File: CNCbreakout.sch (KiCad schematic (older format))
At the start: 90 parts, among them P1 X1, P10 XY_STOP, P11 Z_STOP, P2 X2, P3 Y, P4 Z, P5 VFD_IN, Q1 Q_NPN_CBE, Q10 Q_NPN_CBE, Q12 Q_NPN_CBE, Q2 Q_NPN_CBE, Q3 Q_NPN_CBE, Q4 Q_NPN_CBE, Q6 Q_NPN_CBE, Q8 Q_NPN_CBE

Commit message: added spindle hall, assignd footprints
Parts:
- removed P?: CONN_01X06, symbol CONN_01X06
- added P12: +24V, Connect:bornier2, symbol CONN_01X02
- added P6: VFD_GP1, Connect:bornier2, symbol CONN_01X02
- added P7: VFD_GP2, Connect:bornier2, symbol CONN_01X02
- added P8: VFD_GP3, Connect:bornier2, symbol CONN_01X02
- added P9: GND, Connect:bornier2, symbol CONN_01X02
- added R45, R46: 10K, Resistors_SMD:R_1206, symbol R
- added R50, R51: 100K, Resistors_SMD:R_1206, symbol R
- added U1, U2: 4N25, Opto-Devices:Optocoupler_SMD_ReflowWaveSoldering_KPC357_LTV35x_PC357_SingleChannel, symbol 4N25
- D1, D10, D11, D12, D2, D3, D4, D5, D6, D7, D8, D9: footprint (none) -> LEDs:LED_1206
- D13, D14, D15, D16, D17, D18, D19, D20, D21: renamed from D?; footprint (none) -> LEDs:LED_1206
- P1, P2, P3, P4: footprint (none) -> Connect:DB9FC
- Q1, Q10, Q12, Q2, Q3, Q4, Q6, Q8: footprint (none) -> TO_SOT_Packages_SMD:SOT-23
- Q11, Q13, Q14, Q5, Q7, Q9: renamed from Q?; footprint (none) -> TO_SOT_Packages_SMD:TO-252-2Lead
- R1, R10, R11, R12, R13, R14, R15, R16, R17, R18, R19, R2, R20, R21, R22, R23, R24, R25, R26, R27, R28, R29, R3, R30, R31, R32, R33, R34, R35, R36, R37, R38, R39, R4, R40, R41, R42, R43, R44, R47, R48, R49, R5, R6, R7, R8, R9: renamed from R?; footprint (none) -> Resistors_SMD:R_1206
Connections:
- net labels added: DGND
- net labels removed: ServoOn_CON, ServoOn_PC
- wire segments 216 -> 235
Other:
- note added: "ACS806 Limit switches are 5K NPN base signals intended for 5V."
- note added: "KRS limit switches are optos intended for Open Collector"
- note added: "Servo enable is left to the FPGA."
- note removed: "ACS806 Limit switches are 5V TTL signals."
- note removed: "Intercept the Servo-On signal\nhere to let the safety controller\npower it down."
- note removed: "KRS limit switches are Open Collector"

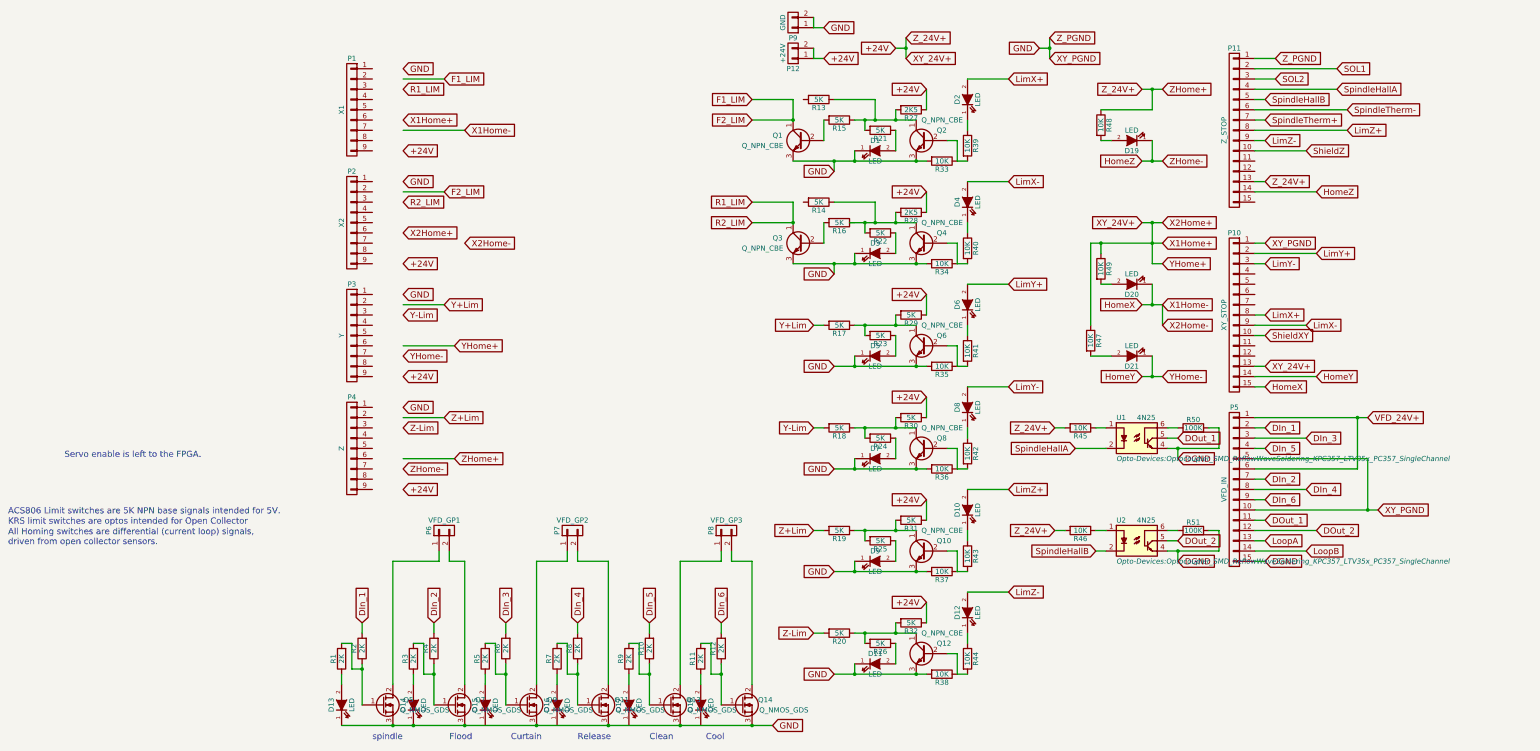
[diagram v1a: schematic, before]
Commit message: cleanup and added enable intercept
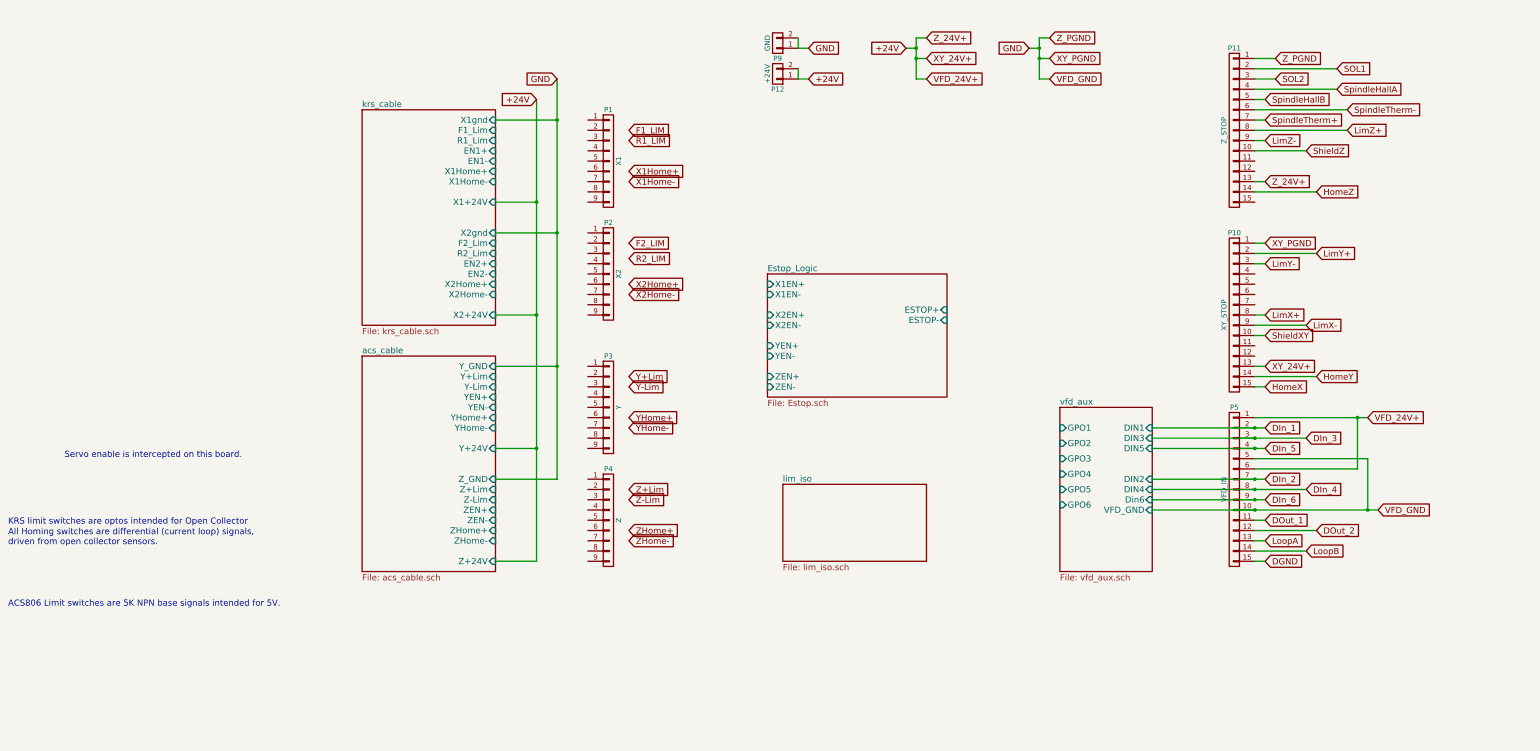
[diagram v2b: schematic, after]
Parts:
- removed D1, D10, D11, D12, D13, D14, D15, D16, D17, D18, D19, D2, D20, D21, D3, D4, D5, D6, D7, D8, D9: LED, LEDs:LED_1206, symbol LED
- removed P6: VFD_GP1, Connect:bornier2, symbol CONN_01X02
- removed P7: VFD_GP2, Connect:bornier2, symbol CONN_01X02
- removed P8: VFD_GP3, Connect:bornier2, symbol CONN_01X02
- removed Q1, Q10, Q12, Q2, Q3, Q4, Q6, Q8: Q_NPN_CBE, TO_SOT_Packages_SMD:SOT-23, symbol Q_NPN_CBE
- removed Q11, Q13, Q14, Q5, Q7, Q9: Q_NMOS_GDS, TO_SOT_Packages_SMD:TO-252-2Lead, symbol Q_NMOS_GDS
- removed R1, R10, R11, R12, R2, R3, R4, R5, R6, R7, R8, R9: 2K, Resistors_SMD:R_1206, symbol R
- removed R13, R14, R15, R16, R17, R18, R19, R20, R21, R22, R23, R24, R25, R26, R29, R30, R31, R32: 5K, Resistors_SMD:R_1206, symbol R
- removed R27, R28: 2K5, Resistors_SMD:R_1206, symbol R
- removed R33, R34, R35, R36, R37, R38, R39, R40, R41, R42, R43, R44, R45, R46, R47, R48, R49: 10K, Resistors_SMD:R_1206, symbol R
- removed R50, R51: 100K, Resistors_SMD:R_1206, symbol R
- removed U1, U2: 4N25, Opto-Devices:Optocoupler_SMD_ReflowWaveSoldering_KPC357_LTV35x_PC357_SingleChannel, symbol 4N25
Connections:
- net VFD_24V+ is gone; now on net +24V: P5.1 (P1), P5.6 (P6)
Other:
- note added: "Servo enable is intercepted on this board."
- note removed: "Clean"
- note removed: "Cool"
- note removed: "Curtain"
- note removed: "Flood"
- note removed: "Release"
- note removed: "Servo enable is left to the FPGA."
- note removed: "spindle"
- moved on the sheet: P1, P12, P2, P3, P4, P9

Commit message: started pcb layout
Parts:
- added P110, P111, P112: CONN_01X02, Connect:bornier2, symbol CONN_01X02
- renumbered P1 to P101, P2 to P102, P3 to P103, P4 to P104, P9 to P105, P12 to P106, P11 to P107, P10 to P108, P5 to P109
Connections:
- net +24V: now also P101.9 (P9), P102.9 (P9), P103.9 (P9), P104.9 (P9)
- net F1_LIM: now also P101.2 (P2)
- net F2_LIM: now also P102.2 (P2)
- net GND: now also P101.1 (P1), P102.1 (P1), P103.1 (P1), P104.1 (P1)
- net R1_LIM: now also P101.3 (P3)
- net R2_LIM: now also P102.3 (P3)
- net X1Home+: now also P101.6 (P6)
- net X1Home-: now also P101.7 (P7)
- net X2Home+: now also P102.6 (P6)
- net X2Home-: now also P102.7 (P7)
- net Y+Lim: now also P103.2 (P2)
- net Y-Lim: now also P103.3 (P3)
- net YHome+: now also P103.6 (P6)
- net YHome-: now also P103.7 (P7)
- net Z+Lim: now also P104.2 (P2)
- net Z-Lim: now also P104.3 (P3)
- net ZHome+: now also P104.6 (P6)
- net ZHome-: now also P104.7 (P7)
- net vfd_aux/GPO1: now also P110.2 (P2)
- net vfd_aux/GPO2: now also P110.1 (P1)
- net vfd_aux/GPO3: now also P111.2 (P2)
- net vfd_aux/GPO4: now also P111.1 (P1)
- net vfd_aux/GPO5: now also P112.2 (P2)
- net vfd_aux/GPO6: now also P112.1 (P1)
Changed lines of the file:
@@
 LimX+
 $Comp
-L CONN_01X15 P11
+L CONN_01X15 P107
 U 1 1 57761910
 P 9300 1700
-F 0 "P11" H 9300 2500 50  0000 C CNN
+F 0 "P107" H 9300 2500 50  0000 C CNN
 F 1 "Z_STOP" V 9400 1700 50  0000 C CNN
 F 2 "" H 9300 1700 50  0001 C CNN
@@
 $EndComp
 $Comp
-L CONN_01X15 P10
+L CONN_01X15 P108
 U 1 1 57761D93
 P 9300 3500
-F 0 "P10" H 9300 4300 50  0000 C CNN
+F 0 "P108" H 9300 4300 50  0000 C CNN
 F 1 "XY_STOP" V 9400 3500 50  0000 C CNN
 F 2 "" H 9300 3500 50  0001 C CNN
@@
 HomeZ
 $Comp
-L CONN_01X15 P5
+L CONN_01X15 P109
 U 1 1 577622EE
 P 9300 5200
-F 0 "P5" H 9300 6000 50  0000 C CNN
+F 0 "P109" H 9300 6000 50  0000 C CNN
 F 1 "VFD_IN" V 9400 5200 50  0000 C CNN
 F 2 "" H 9300 5200 50  0001 C CNN
@@
 ShieldXY
 $Comp
-L CONN_01X09 P1
+L CONN_01X09 P101
 U 1 1 57762AFC
 P 3200 2000
-F 0 "P1" H 3200 2500 50  0000 C CNN
+F 0 "P101" H 3200 2500 50  0000 C CNN
 F 1 "X1" V 3300 2000 50  0000 C CNN
 F 2 "Connect:DB9FC" H 3200 2000 50  0001 C CNN
@@
 $EndComp
 $Comp
-L CONN_01X09 P2
+L CONN_01X09 P102
 U 1 1 57762B71
 P 3200 3100
-F 0 "P2" H 3200 3600 50  0000 C CNN
+F 0 "P102" H 3200 3600 50  0000 C CNN
 F 1 "X2" V 3300 3100 50  0000 C CNN
 F 2 "Connect:DB9FC" H 3200 3100 50  0001 C CNN
@@
 $EndComp
 $Comp
-L CONN_01X09 P3
+L CONN_01X09 P103
 U 1 1 57762BB0
 P 3200 4400
-F 0 "P3" H 3200 4900 50  0000 C CNN
+F 0 "P103" H 3200 4900 50  0000 C CNN
 F 1 "Y" V 3300 4400 50  0000 C CNN
 F 2 "Connect:DB9FC" H 3200 4400 50  0001 C CNN
@@
 $EndComp
 $Comp
-L CONN_01X09 P4
+L CONN_01X09 P104
 U 1 1 57762BE4
 P 3200 5500
-F 0 "P4" H 3200 6000 50  0000 C CNN
+F 0 "P104" H 3200 6000 50  0000 C CNN
 F 1 "Z" V 3300 5500 50  0000 C CNN
 F 2 "Connect:DB9FC" H 3200 5500 50  0001 C CNN
@@
 Text Notes -2650 6350 0    60   ~ 0
 ACS806 Limit switches are 5K NPN base signals intended for 5V.
-Text Notes -2650 5550 0    60   ~ 0
+Text Notes -2650 6250 0    60   ~ 0
 KRS limit switches are optos intended for Open Collector
 Text Notes -2650 5750 0    60   ~ 0
@@
 DGND
 $Comp
-L CONN_01X02 P9
+L CONN_01X02 P105
 U 1 1 57895CA5
 P 4850 850
-F 0 "P9" H 4850 1000 50  0000 C CNN
+F 0 "P105" H 4850 1000 50  0000 C CNN
 F 1 "GND" V 4950 850 50  0000 C CNN
 F 2 "Connect:bornier2" H 4850 850 50  0001 C CNN
@@
 $EndComp
 $Comp
-L CONN_01X02 P12
+L CONN_01X02 P106
 U 1 1 578983DE
 P 4850 1150
-F 0 "P12" H 4850 1300 50  0000 C CNN
+F 0 "P106" H 4850 1300 50  0000 C CNN
 F 1 "+24V" V 4950 1150 50  0000 C CNN
 F 2 "Connect:bornier2" H 4850 1150 50  0001 C CNN
@@
 Text Notes -2100 4900 0    60   ~ 0
 Servo enable is intercepted on this board.
-Text GLabel 3400 2950 2    60   Input ~ 0
+Text GLabel 3400 2900 2    60   Input ~ 0
 R2_LIM
 Text GLabel 6300 1200 2    60   Input ~ 0
@@
 Connection ~ 2500 2400
 Wire Wire Line
-	2700 2700 2100 2700
-Wire Wire Line
-	2500 3500 2100 3500
-Wire Wire Line
-	2500 5900 2100 5900
+	2100 2700 3000 2700
+Wire Wire Line
+	2100 3500 3000 3500
+Wire Wire Line
+	2100 5900 3000 5900
 Connection ~ 2500 3500
 Wire Wire Line
-	2100 4800 2500 4800
+	2100 4800 3000 4800
 Connection ~ 2500 4800
 Wire Wire Line
-	2700 4000 2100 4000
+	2100 4000 3000 4000
 Connection ~ 2700 2700
 Wire Wire Line
-	2700 5100 2100 5100
+	2100 5100 3000 5100
 Connection ~ 2700 4000
 Wire Wire Line
-	2100 1600 2700 1600
-Wire Wire Line
-	2100 2400 2500 2400
+	2100 1600 3000 1600
+Wire Wire Line
+	2100 2400 3000 2400
 Connection ~ 9500 5400
 Connection ~ 9500 5300
@@
 	7400 1200 7500 1200
 Connection ~ 7400 1000
+Wire Wire Line
+	3400 1700 3000 1700
+Wire Wire Line
+	3000 1800 3400 1800
+Wire Wire Line
+	3400 2100 3000 2100
+Wire Wire Line
+	3000 2200 3400 2200
+Wire Wire Line
+	3400 2800 3000 2800
+Wire Wire Line
+	3400 3200 3000 3200
+Wire Wire Line
+	3000 3300 3400 3300
+Wire Wire Line
+	3400 2900 3000 2900
+Wire Wire Line
+	3400 4100 3000 4100
+Wire Wire Line
+	3000 4200 3400 4200
+Wire Wire Line
+	3400 4500 3000 4500
+Wire Wire Line
+	3000 4600 3400 4600
+Connection ~ 2700 5100
+Wire Wire Line
+	3000 5200 3400 5200
+Wire Wire Line
+	3400 5300 3000 5300
+Wire Wire Line
+	3000 5600 3400 5600
+Wire Wire Line
+	3400 5700 3000 5700
+Connection ~ 2500 5900
+$Comp
+L CONN_01X02 P110
+U 1 1 57B63261
+P 7150 4650
+F 0 "P110" H 7150 4800 50  0000 C CNN
+F 1 "CONN_01X02" V 7250 4650 50  0000 C CNN
+F 2 "Connect:bornier2" H 7150 4650 50  0001 C CNN
+F 3 "" H 7150 4650 50  0000 C CNN
+	1    7150 4650
+	-1   0    0    1
+$EndComp
+$Comp
+L CONN_01X02 P111
+U 1 1 57B63643
+P 7150 4950
+F 0 "P111" H 7150 5100 50  0000 C CNN
+F 1 "CONN_01X02" V 7250 4950 50  0000 C CNN
+F 2 "Connect:bornier2" H 7150 4950 50  0001 C CNN
+F 3 "" H 7150 4950 50  0000 C CNN
+	1    7150 4950
+	-1   0    0    1
+$EndComp
+$Comp
+L CONN_01X02 P112
+U 1 1 57B637C6
+P 7150 5250
+F 0 "P112" H 7150 5400 50  0000 C CNN
+F 1 "CONN_01X02" V 7250 5250 50  0000 C CNN
+F 2 "Connect:bornier2" H 7150 5250 50  0001 C CNN
+F 3 "" H 7150 5250 50  0000 C CNN
+	1    7150 5250
+	-1   0    0    1
+$EndComp
+Wire Wire Line
+	7350 4600 7600 4600
+Wire Wire Line
+	7600 4750 7350 4750
+Wire Wire Line
+	7350 4750 7350 4700
+Wire Wire Line
+	7350 4900 7600 4900
+Wire Wire Line
+	7600 5050 7350 5050
+Wire Wire Line
+	7350 5050 7350 5000
+Wire Wire Line
+	7350 5200 7600 5200
+Wire Wire Line
+	7600 5350 7350 5350
+Wire Wire Line
+	7350 5350 7350 5300
 $EndSCHEMATC

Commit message: added opto and DE footprints
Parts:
- P101, P102, P103, P104: footprint Connect:DB9FC -> CNCbreakout:DE9FC
- P107, P108, P109: footprint (none) -> CNCbreakout:DE15HDFC
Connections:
- net Estop_Logic/X1EN+: now also P101.4 (P4)
- net Estop_Logic/X1EN-: now also P101.5 (P5)
- net Estop_Logic/X2EN+: now also P102.4 (P4)
- net Estop_Logic/X2EN-: now also P102.5 (P5)
- net Estop_Logic/YEN+: now also P103.4 (P4)
- net Estop_Logic/YEN-: now also P103.5 (P5)
- net Estop_Logic/ZEN+: now also P104.4 (P4)
- net Estop_Logic/ZEN-: now also P104.5 (P5)
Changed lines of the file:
@@
 LIBS:valves
 LIBS:references
+LIBS:FabLab
 LIBS:CNCbreakout-cache
 EELAYER 25 0
@@
 F 0 "P107" H 9300 2500 50  0000 C CNN
 F 1 "Z_STOP" V 9400 1700 50  0000 C CNN
-F 2 "" H 9300 1700 50  0001 C CNN
+F 2 "CNCbreakout:DE15HDFC" H 9300 1700 50  0001 C CNN
 F 3 "" H 9300 1700 50  0000 C CNN
 	1    9300 1700
@@
 F 0 "P108" H 9300 4300 50  0000 C CNN
 F 1 "XY_STOP" V 9400 3500 50  0000 C CNN
-F 2 "" H 9300 3500 50  0001 C CNN
+F 2 "CNCbreakout:DE15HDFC" H 9300 3500 50  0001 C CNN
 F 3 "" H 9300 3500 50  0000 C CNN
 	1    9300 3500
@@
 F 0 "P109" H 9300 6000 50  0000 C CNN
 F 1 "VFD_IN" V 9400 5200 50  0000 C CNN
-F 2 "" H 9300 5200 50  0001 C CNN
+F 2 "CNCbreakout:DE15HDFC" H 9300 5200 50  0001 C CNN
 F 3 "" H 9300 5200 50  0000 C CNN
 	1    9300 5200
@@
 F 0 "P101" H 3200 2500 50  0000 C CNN
 F 1 "X1" V 3300 2000 50  0000 C CNN
-F 2 "Connect:DB9FC" H 3200 2000 50  0001 C CNN
+F 2 "CNCbreakout:DE9FC" H 3200 2000 50  0001 C CNN
 F 3 "" H 3200 2000 50  0000 C CNN
 	1    3200 2000
@@
 F 0 "P102" H 3200 3600 50  0000 C CNN
 F 1 "X2" V 3300 3100 50  0000 C CNN
-F 2 "Connect:DB9FC" H 3200 3100 50  0001 C CNN
+F 2 "CNCbreakout:DE9FC" H 3200 3100 50  0001 C CNN
 F 3 "" H 3200 3100 50  0000 C CNN
 	1    3200 3100
@@
 F 0 "P103" H 3200 4900 50  0000 C CNN
 F 1 "Y" V 3300 4400 50  0000 C CNN
-F 2 "Connect:DB9FC" H 3200 4400 50  0001 C CNN
+F 2 "CNCbreakout:DE9FC" H 3200 4400 50  0001 C CNN
 F 3 "" H 3200 4400 50  0000 C CNN
 	1    3200 4400
@@
 F 0 "P104" H 3200 6000 50  0000 C CNN
 F 1 "Z" V 3300 5500 50  0000 C CNN
-F 2 "Connect:DB9FC" H 3200 5500 50  0001 C CNN
+F 2 "CNCbreakout:DE9FC" H 3200 5500 50  0001 C CNN
 F 3 "" H 3200 5500 50  0000 C CNN
 	1    3200 5500
@@
 Wire Wire Line
 	7350 5350 7350 5300
+Wire Wire Line
+	4750 3200 4600 3200
+Wire Wire Line
+	4600 3200 4600 1900
+Wire Wire Line
+	4600 1900 3000 1900
+Wire Wire Line
+	3000 2000 4500 2000
+Wire Wire Line
+	4500 2000 4500 3300
+Wire Wire Line
+	4500 3300 4750 3300
+Wire Wire Line
+	4750 3500 4400 3500
+Wire Wire Line
+	4400 3500 4400 3000
+Wire Wire Line
+	4400 3000 3000 3000
+Wire Wire Line
+	3000 3100 4300 3100
+Wire Wire Line
+	4300 3100 4300 3600
+Wire Wire Line
+	4300 3600 4750 3600
+Wire Wire Line
+	4750 3800 4300 3800
+Wire Wire Line
+	4300 3800 4300 4300
+Wire Wire Line
+	4300 4300 3000 4300
+Wire Wire Line
+	3000 4400 4400 4400
+Wire Wire Line
+	4400 4400 4400 3900
+Wire Wire Line
+	4400 3900 4750 3900
+Wire Wire Line
+	4750 4100 4500 4100
+Wire Wire Line
+	4500 4100 4500 5400
+Wire Wire Line
+	4500 5400 3000 5400
+Wire Wire Line
+	3000 5500 4600 5500
+Wire Wire Line
+	4600 5500 4600 4200
+Wire Wire Line
+	4600 4200 4750 4200
 $EndSCHEMATC

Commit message: set limits to pull down, optional invert
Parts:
- renumbered P110 to P107, P111 to P108, P112 to P109, P107 to P110, P108 to P111, P109 to P112
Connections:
- net X1Home+: no longer names the net of P101.6 (P6)
- net X2Home+: no longer names the net of P102.6 (P6)
- net YHome+: no longer names the net of P103.6 (P6)
- net ZHome+: no longer names the net of P104.6 (P6)
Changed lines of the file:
@@
 LimX+
 $Comp
-L CONN_01X15 P107
+L CONN_01X15 P110
 U 1 1 57761910
 P 9300 1700
-F 0 "P107" H 9300 2500 50  0000 C CNN
+F 0 "P110" H 9300 2500 50  0000 C CNN
 F 1 "Z_STOP" V 9400 1700 50  0000 C CNN
 F 2 "CNCbreakout:DE15HDFC" H 9300 1700 50  0001 C CNN
@@
 $EndComp
 $Comp
-L CONN_01X15 P108
+L CONN_01X15 P111
 U 1 1 57761D93
 P 9300 3500
-F 0 "P108" H 9300 4300 50  0000 C CNN
+F 0 "P111" H 9300 4300 50  0000 C CNN
 F 1 "XY_STOP" V 9400 3500 50  0000 C CNN
 F 2 "CNCbreakout:DE15HDFC" H 9300 3500 50  0001 C CNN
@@
 HomeZ
 $Comp
-L CONN_01X15 P109
+L CONN_01X15 P112
 U 1 1 577622EE
 P 9300 5200
-F 0 "P109" H 9300 6000 50  0000 C CNN
+F 0 "P112" H 9300 6000 50  0000 C CNN
 F 1 "VFD_IN" V 9400 5200 50  0000 C CNN
 F 2 "CNCbreakout:DE15HDFC" H 9300 5200 50  0001 C CNN
@@
 Text GLabel 3400 5300 2    60   Input ~ 0
 Z-Lim
-Text GLabel 3400 2100 2    60   Input ~ 0
-X1Home+
 Text GLabel 3400 2200 2    60   Input ~ 0
 X1Home-
@@
 Text Notes -2650 5750 0    60   ~ 0
 All Homing switches are differential (current loop) signals,\ndriven from open collector sensors.
-Text GLabel 3400 3200 2    60   Input ~ 0
-X2Home+
 Text GLabel 3400 3300 2    60   Input ~ 0
 X2Home-
-Text GLabel 3400 4500 2    60   Input ~ 0
-YHome+
 Text GLabel 3400 4600 2    60   Input ~ 0
 YHome-
-Text GLabel 3400 5600 2    60   Input ~ 0
-ZHome+
 Text GLabel 3400 5700 2    60   Input ~ 0
 ZHome-
@@
 F5 "YEN+" I R 2100 4300 60
 F6 "YEN-" I R 2100 4400 60
-F7 "YHome+" I R 2100 4500 60
-F8 "YHome-" I R 2100 4600 60
-F9 "Y+24V" I R 2100 4800 60
-F10 "Z_GND" I R 2100 5100 60
-F11 "Z+Lim" I R 2100 5200 60
-F12 "Z-Lim" I R 2100 5300 60
-F13 "ZEN+" I R 2100 5400 60
-F14 "ZEN-" I R 2100 5500 60
-F15 "ZHome+" I R 2100 5600 60
-F16 "ZHome-" I R 2100 5700 60
-F17 "Z+24V" I R 2100 5900 60
+F7 "YHome-" I R 2100 4600 60
+F8 "Y+24V" I R 2100 4800 60
+F9 "Z_GND" I R 2100 5100 60
+F10 "Z+Lim" I R 2100 5200 60
+F11 "Z-Lim" I R 2100 5300 60
+F12 "ZEN+" I R 2100 5400 60
+F13 "ZEN-" I R 2100 5500 60
+F14 "ZHome-" I R 2100 5700 60
+F15 "Z+24V" I R 2100 5900 60
 $EndSheet
 $Sheet
@@
 F5 "EN1+" I R 2100 1900 60
 F6 "EN1-" I R 2100 2000 60
-F7 "X1Home+" I R 2100 2100 60
-F8 "X1Home-" I R 2100 2200 60
-F9 "X1+24V" I R 2100 2400 60
-F10 "X2gnd" I R 2100 2700 60
-F11 "F2_Lim" I R 2100 2800 60
-F12 "R2_Lim" I R 2100 2900 60
-F13 "EN2+" I R 2100 3000 60
-F14 "EN2-" I R 2100 3100 60
-F15 "X2Home+" I R 2100 3200 60
-F16 "X2Home-" I R 2100 3300 60
-F17 "X2+24V" I R 2100 3500 60
+F7 "X1Home-" I R 2100 2200 60
+F8 "X1+24V" I R 2100 2400 60
+F9 "X2gnd" I R 2100 2700 60
+F10 "F2_Lim" I R 2100 2800 60
+F11 "R2_Lim" I R 2100 2900 60
+F12 "EN2+" I R 2100 3000 60
+F13 "EN2-" I R 2100 3100 60
+F14 "X2Home-" I R 2100 3300 60
+F15 "X2+24V" I R 2100 3500 60
 $EndSheet
 Text Notes -2100 4900 0    60   ~ 0
@@
 	3000 1800 3400 1800
 Wire Wire Line
-	3400 2100 3000 2100
-Wire Wire Line
 	3000 2200 3400 2200
 Wire Wire Line
 	3400 2800 3000 2800
 Wire Wire Line
-	3400 3200 3000 3200
-Wire Wire Line
 	3000 3300 3400 3300
 Wire Wire Line
@@
 Wire Wire Line
 	3000 4200 3400 4200
-Wire Wire Line
-	3400 4500 3000 4500
 Wire Wire Line
 	3000 4600 3400 4600
@@
 	3400 5300 3000 5300
 Wire Wire Line
-	3000 5600 3400 5600
-Wire Wire Line
 	3400 5700 3000 5700
 Connection ~ 2500 5900
 $Comp
-L CONN_01X02 P110
+L CONN_01X02 P107
 U 1 1 57B63261
 P 7150 4650
-F 0 "P110" H 7150 4800 50  0000 C CNN
+F 0 "P107" H 7150 4800 50  0000 C CNN
 F 1 "CONN_01X02" V 7250 4650 50  0000 C CNN
 F 2 "Connect:bornier2" H 7150 4650 50  0001 C CNN
@@
 $EndComp
 $Comp
-L CONN_01X02 P111
+L CONN_01X02 P108
 U 1 1 57B63643
 P 7150 4950
-F 0 "P111" H 7150 5100 50  0000 C CNN
+F 0 "P108" H 7150 5100 50  0000 C CNN
 F 1 "CONN_01X02" V 7250 4950 50  0000 C CNN
 F 2 "Connect:bornier2" H 7150 4950 50  0001 C CNN
@@
 $EndComp
 $Comp
-L CONN_01X02 P112
+L CONN_01X02 P109
 U 1 1 57B637C6
 P 7150 5250
-F 0 "P112" H 7150 5400 50  0000 C CNN
+F 0 "P109" H 7150 5400 50  0000 C CNN
 F 1 "CONN_01X02" V 7250 5250 50  0000 C CNN
 F 2 "Connect:bornier2" H 7150 5250 50  0001 C CNN
